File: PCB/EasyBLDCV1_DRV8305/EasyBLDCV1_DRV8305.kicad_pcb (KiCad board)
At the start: 4 copper layers, 46.9 x 46.7 mm, 73 parts, among them J1 10159560-A00221RLF, J2 TC2050-IDC, Q1 CSD16556Q5B, Q2 CSD16556Q5B, Q3 CSD16556Q5B, Q4 CSD16556Q5B, Q5 CSD16556Q5B, Q6 CSD16556Q5B, U1 DRV83053PHP, U2 TMS320F28027FPTT, U3 TPD4E05U06DQAR, U4 LMR16006XDDCR

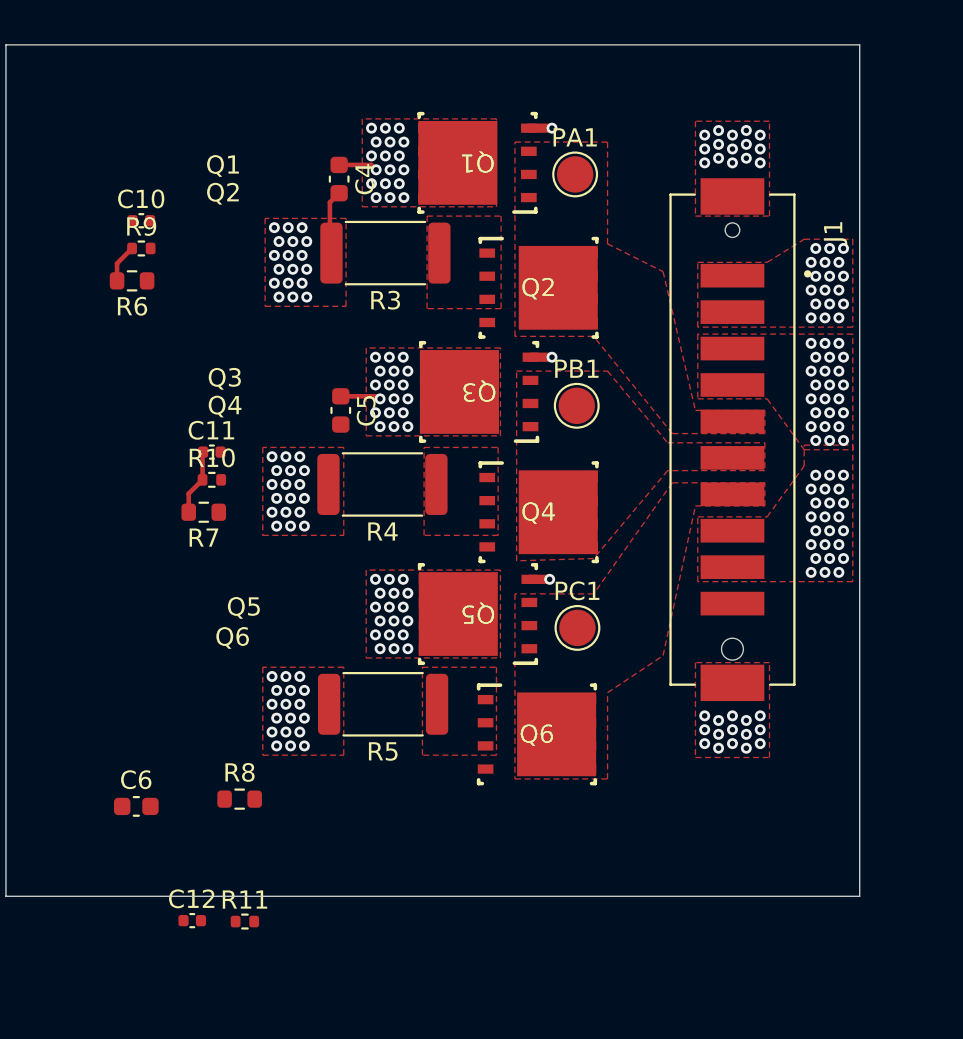
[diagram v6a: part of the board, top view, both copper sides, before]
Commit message: Finished Mosfet Layout
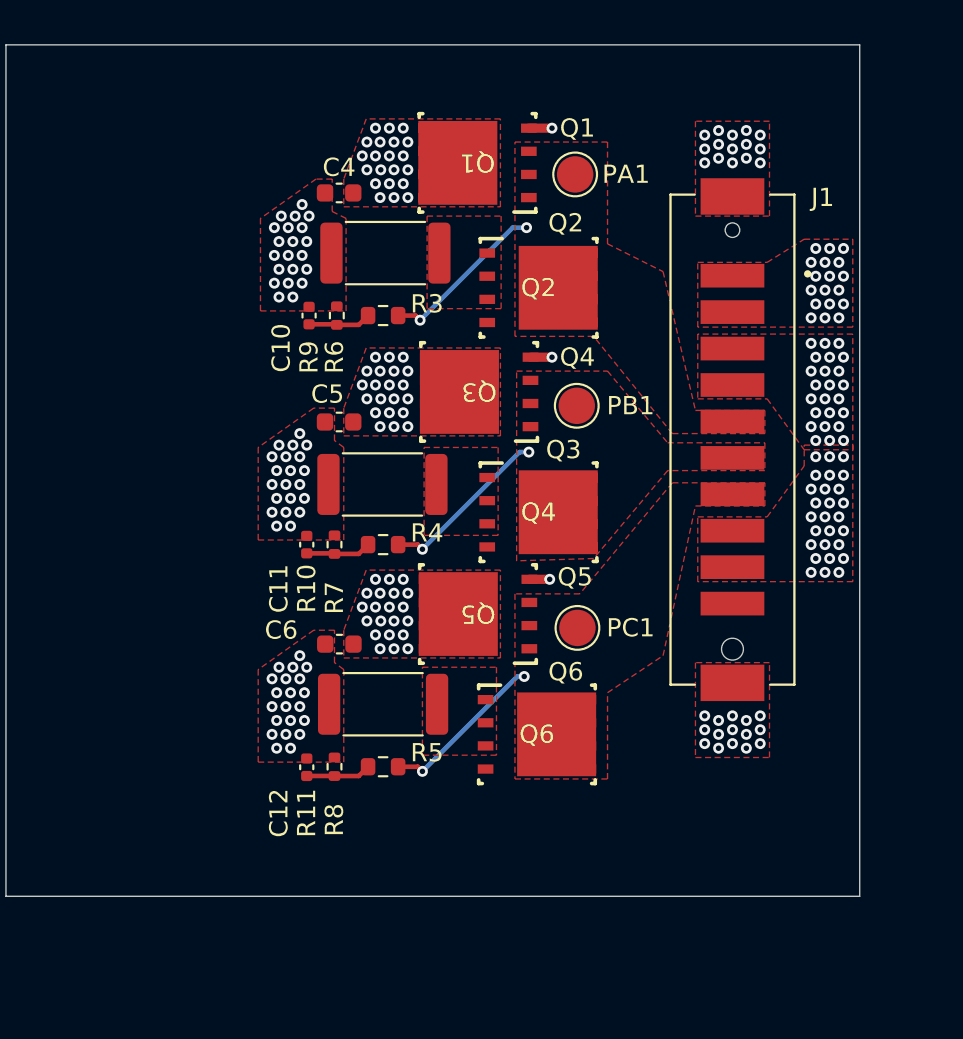
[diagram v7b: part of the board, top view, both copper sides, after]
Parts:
- moved C6 14.3 mm to (218.5, 155.8), turned to 180 degrees
- moved R6 13.9 mm to (220.9, 137.8)
- moved R9 11.3 mm to (218.3, 137.8), turned to 90 degrees
- moved C10 10.6 mm to (216.8, 137.8), turned to 90 degrees
- moved C12 10.5 mm to (216.7, 162.6), turned to 90 degrees
- moved R7 10.0 mm to (220.9, 150.4)
- moved R11 9.82 mm to (218.2, 162.6), turned to 90 degrees
- moved R8 8.07 mm to (220.9, 162.6), turned to 180 degrees
- moved R10 7.61 mm to (218.2, 150.4), turned to 90 degrees
- moved C11 7.28 mm to (216.7, 150.4), turned to 90 degrees
- moved C4 0.76 mm to (218.4, 131.1), turned to 180 degrees
- moved C5 0.64 mm to (218.4, 143.6), turned to 180 degrees
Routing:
- net MOT_B: track 0.00 -> 9.49 mm, vias 0 -> 2
- net MOT_A: track 0.00 -> 9.26 mm, vias 0 -> 2
- net MOT_C: track 0.00 -> 9.18 mm, vias 0 -> 2
- net PVDD: track 25.6 -> 21.0 mm, vias 76 -> 85
- net VSEN_C: track 3.52 -> 7.10 mm
- net GND: track 75.2 -> 71.6 mm, vias 155 -> 167
- net VSEN_A: track 5.65 -> 7.00 mm

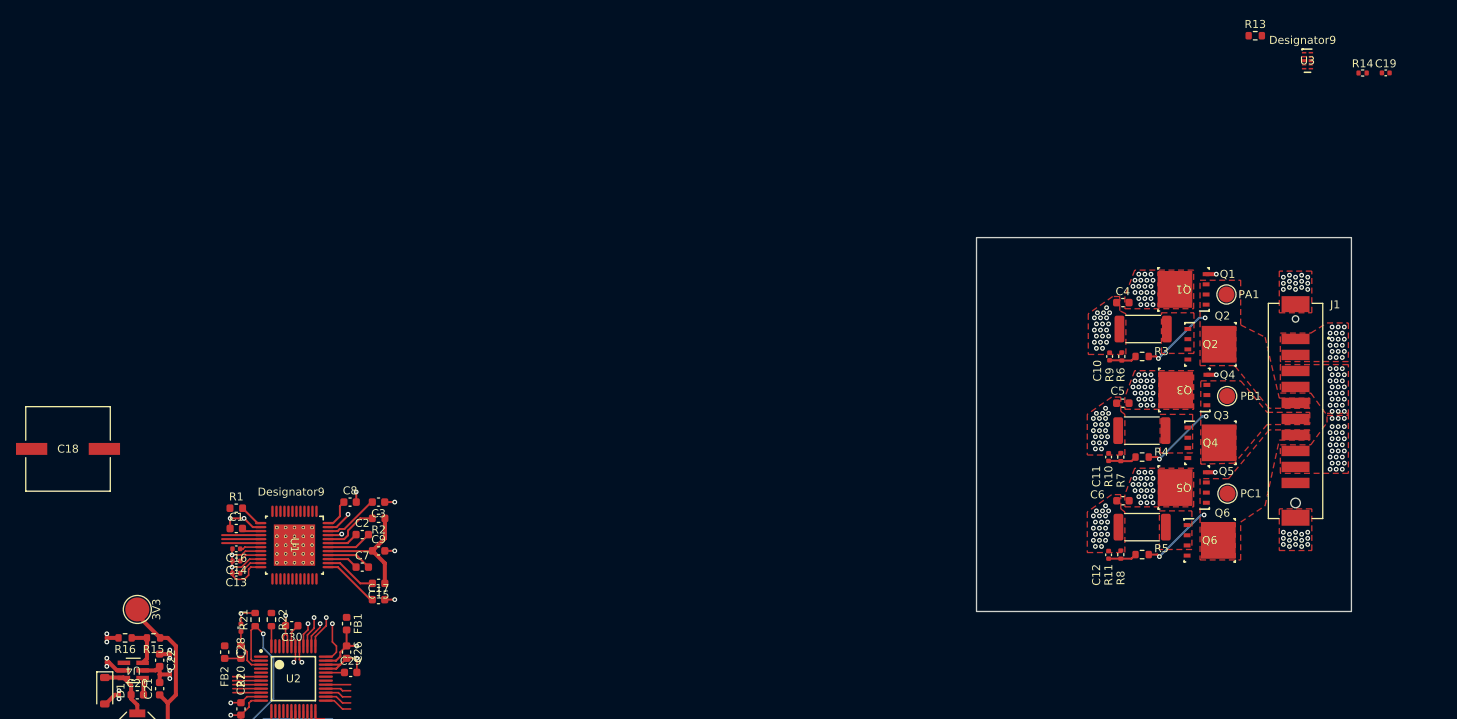
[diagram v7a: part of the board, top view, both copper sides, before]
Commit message: Started layout between drv and fets
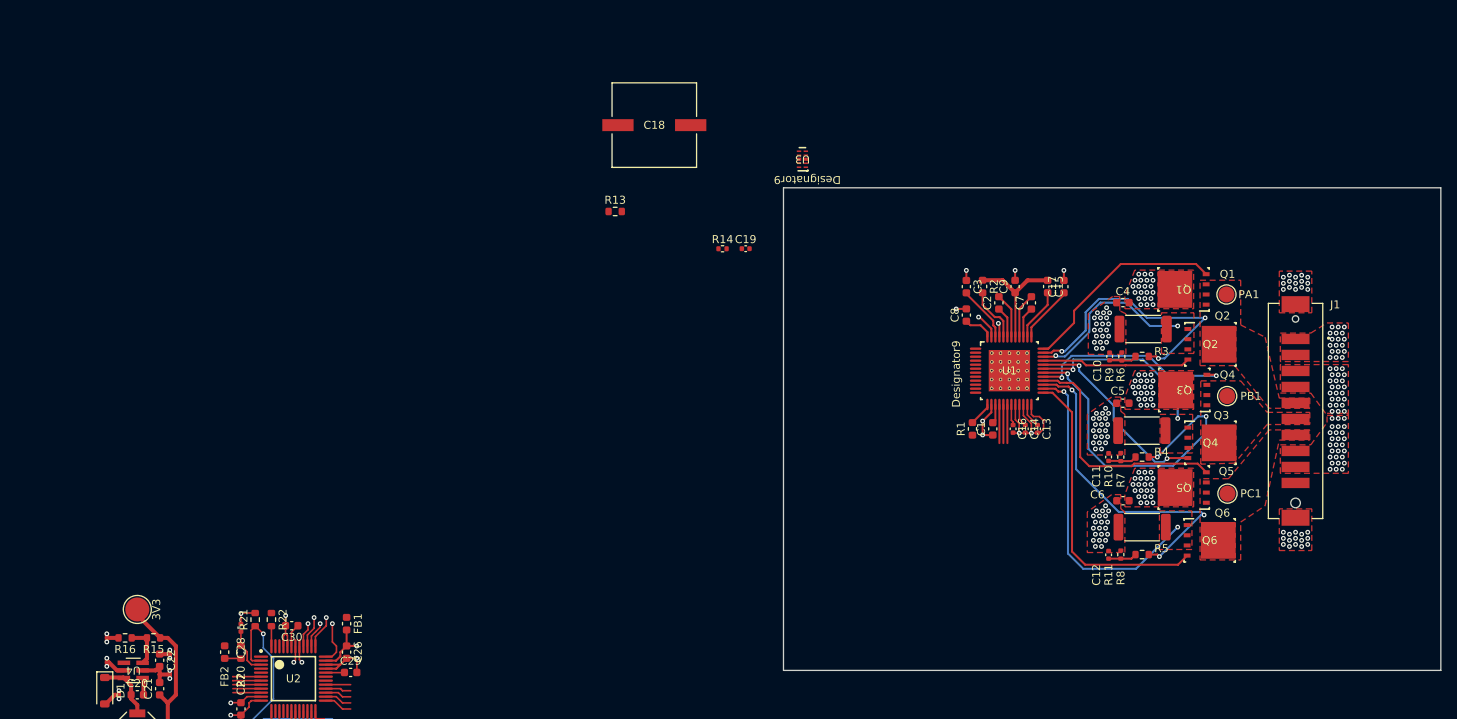
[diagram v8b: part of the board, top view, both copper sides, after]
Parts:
- moved C13 101.8 mm to (207.8, 146.8), turned to -90 degrees
- moved C14 100.0 mm to (206.2, 146.8), turned to -90 degrees
- moved C16 98.2 mm to (204.7, 146.8), turned to -90 degrees
- moved C1 95.4 mm to (202.2, 146.8), turned to 90 degrees
- moved C17 94.2 mm to (211.1, 129.1), turned to 90 degrees
- moved R1 92.6 mm to (199.6, 146.8), turned to 90 degrees
- moved U1 92.0 mm to (204.3, 139.6), turned to 0 degrees
- moved C15 91.5 mm to (209.0, 129.1), turned to -90 degrees
- moved C7 89.9 mm to (207.0, 131.1), turned to 90 degrees
- moved C9 86.2 mm to (205.0, 129.1), turned to 90 degrees
- moved C2 84.7 mm to (202.9, 131.1), turned to 90 degrees
- moved C18 83.7 mm to (159.9, 108.9)
- moved C19 83.0 mm to (171.3, 124.3)
- moved R13 83.0 mm to (155.0, 119.7)
- moved R14 83.0 mm to (168.4, 124.3)
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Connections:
- U1 pad V: (no net) -> GND
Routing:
- net SL_C: track 2.65 -> 42.5 mm, vias 0 -> 2
- net GL_C: track 0.00 -> 37.6 mm
- net MOT_B: track 9.49 -> 42.2 mm, vias 2 -> 3
- net MOT_C: track 9.18 -> 41.5 mm, vias 2 -> 3
- net GH_C: track 1.12 -> 30.3 mm, vias 1 -> 0
- net MOT_A: track 9.26 -> 34.7 mm, vias 2 -> 3
- net GH_A: track 1.27 -> 26.2 mm, vias 1 -> 0
- net GL_B: track 0.00 -> 24.8 mm, vias 0 -> 2
- net GH_B: track 1.18 -> 26.0 mm, vias 1 -> 2
- net SL_B: track 2.87 -> 25.8 mm, vias 0 -> 2
- net SL_A: track 3.09 -> 25.3 mm, vias 0 -> 2
- net GL_A: track 0.00 -> 18.6 mm
- added copper zone on In2.Cu, net GND
- added copper zone on In1.Cu, net PVDD
- removed copper zone on In1.Cu, net GND
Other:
- board size 46.9 x 46.7 mm -> 82.2 x 60.3 mm
